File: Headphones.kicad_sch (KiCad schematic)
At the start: 34 parts, among them IC2 MAX9744ETH+T, IC3 UDA1334ATS_N2,118, U1 MOUDLE-SEEEDUINO-XIAO-ESP32C3

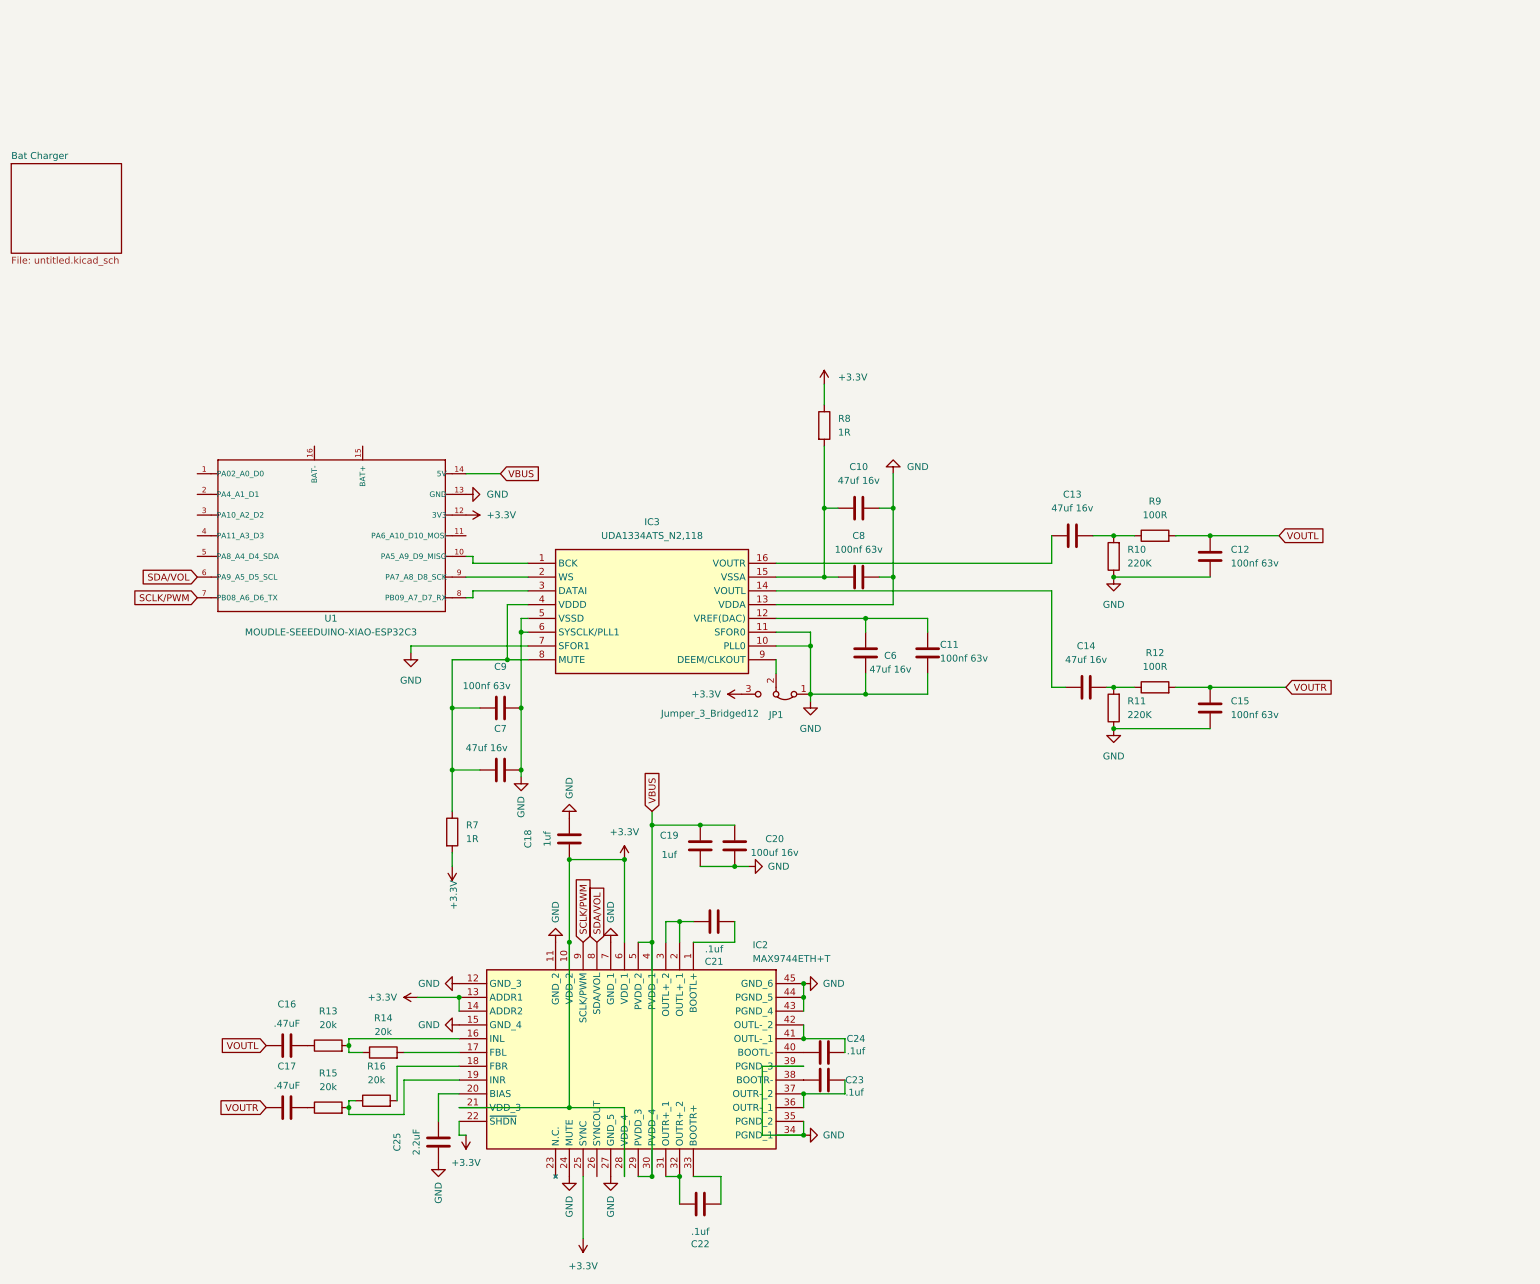
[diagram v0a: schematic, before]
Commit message: Minor updates
Might need more room for the esp32. With the new USB connector the board space is very tight
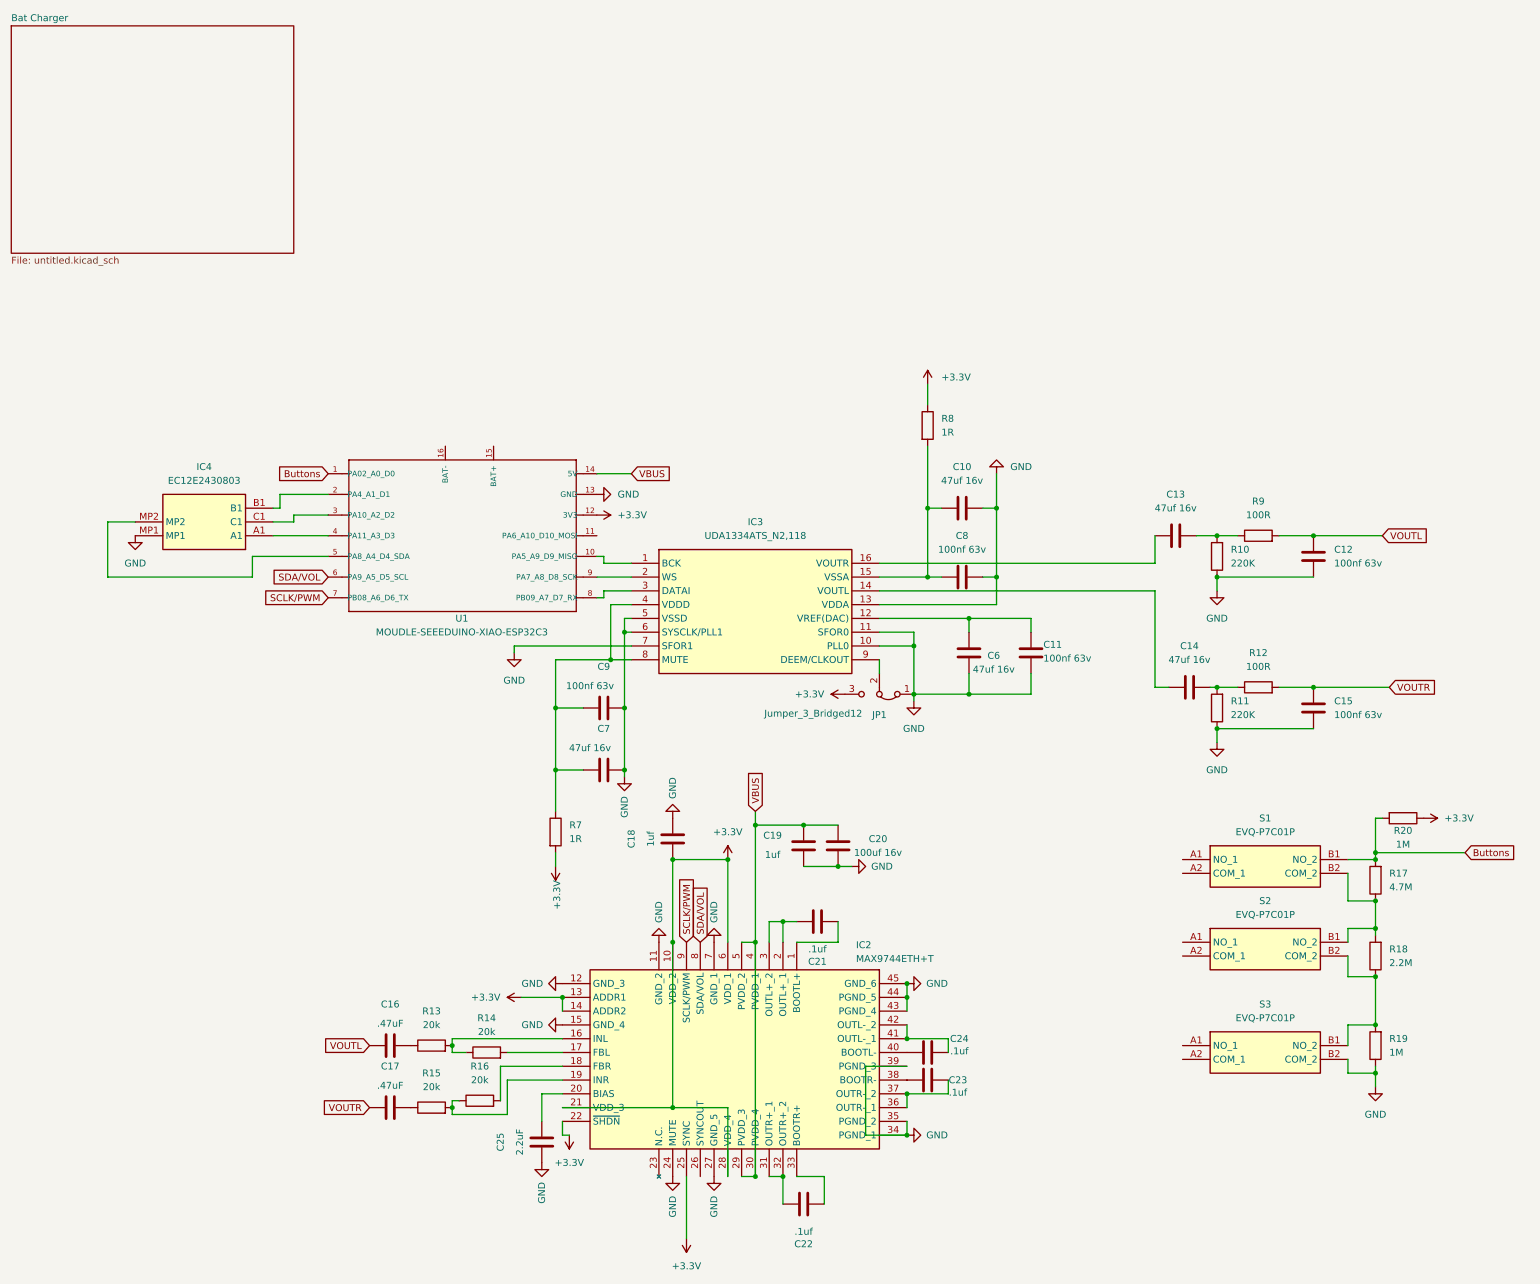
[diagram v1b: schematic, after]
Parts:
- added IC4: EC12E2430803, EC12E2430803, symbol SamacSys_Parts:EC12E2430803
- added R17: 4.7M, Resistor_SMD:R_0805_2012Metric, symbol Device:R
- added R18: 2.2M, Resistor_SMD:R_0805_2012Metric, symbol Device:R
- added R19, R20: 1M, Resistor_SMD:R_0805_2012Metric, symbol Device:R
- added S1, S2, S3: EVQ-P7C01P, EVQP7C01P, symbol SamacSys_Parts:EVQ-P7C01P
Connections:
- net +3.3V: now also R20.1
- net GND: now also IC4.MP1, R19.1, S3.B2 (COM_2)
- net Buttons: now reaches U1.1 (PA02_A0_D0)
- net Buttons: now also R17.2, R20.2, S1.B1 (NO_2)
- net at U1.2 (PA4_A1_D1): now also IC4.B1
- net at U1.3 (PA10_A2_D2): now also IC4.C1
- net at U1.4 (PA11_A3_D3): now also IC4.A1
- net at U1.5 (PA8_A4_D4_SDA): now also IC4.MP2
- new net: R18.1, R19.2, S2.B2 (COM_2), S3.B1 (NO_2)
- new net: R17.1, R18.2, S1.B2 (COM_2), S2.B1 (NO_2)
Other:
- moved on the sheet: C10, C11, C12, C13, C14, C15, C16, C17, C18, C19, C20, C21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

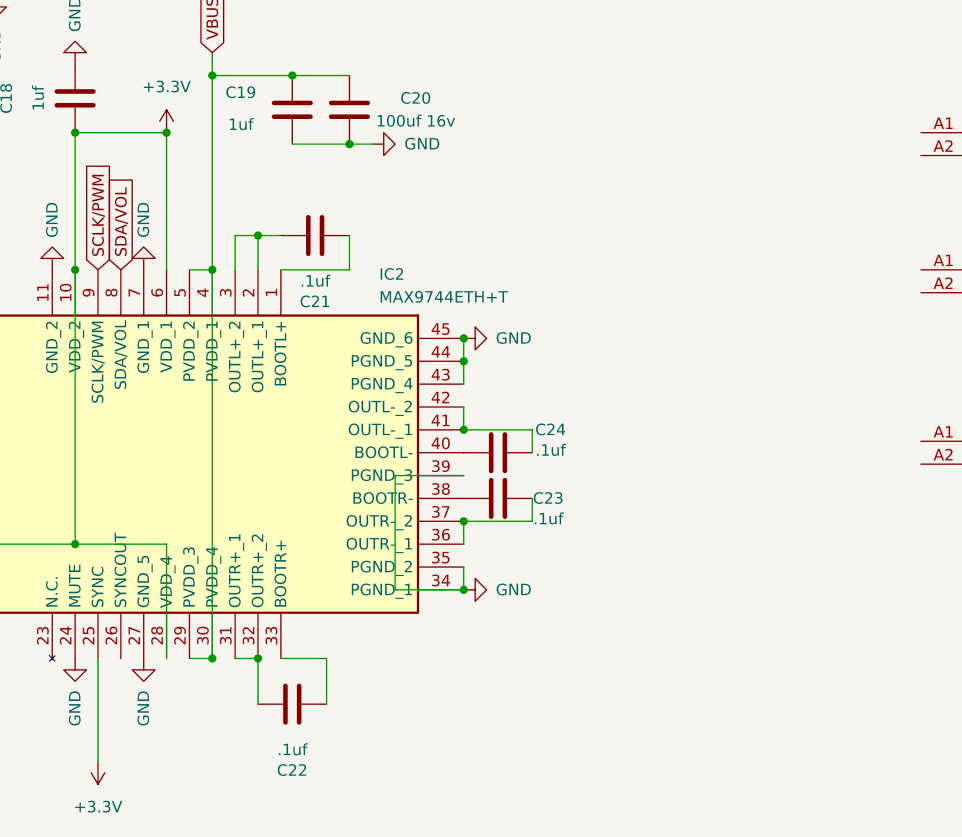
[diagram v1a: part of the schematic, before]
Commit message: Rev1 Update
Layout and traces done. 3d model done. Need to review layout placement and schematic. Change amp and dsp for lower cost??
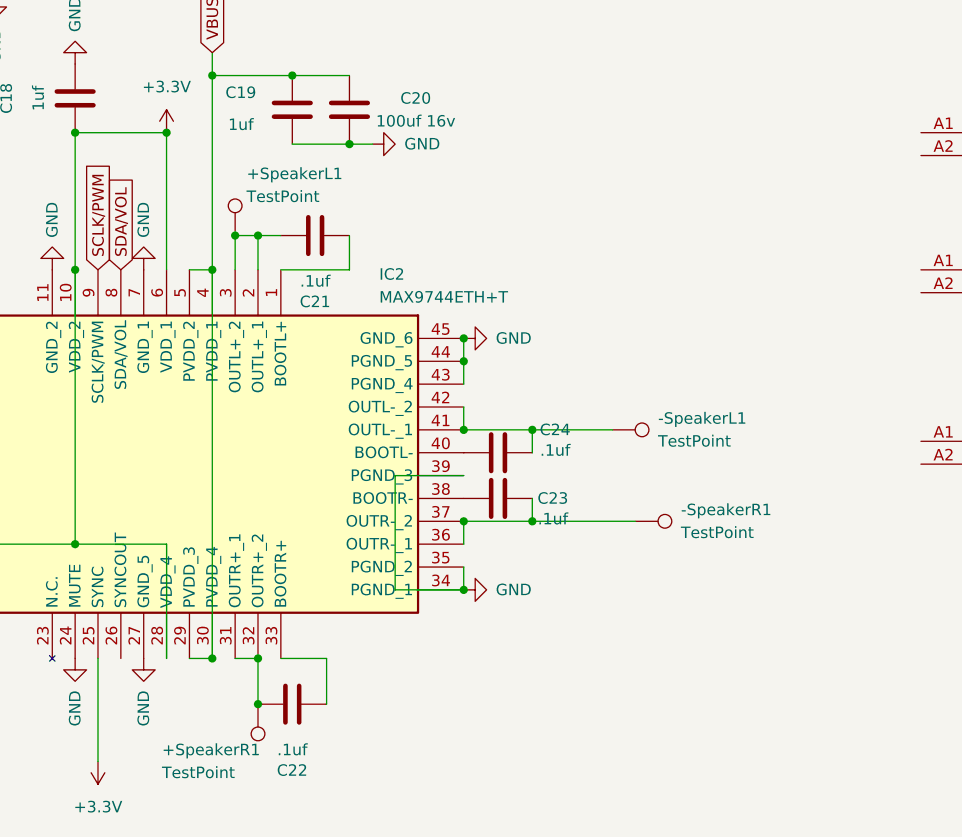
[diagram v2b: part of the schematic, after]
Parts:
- added +SpeakerL1, +SpeakerR1, -SpeakerL1, -SpeakerR1: TestPoint, TestPoint:TestPoint_Loop_D1.80mm_Drill1.0mm_Beaded, symbol Connector:TestPoint
- R7, R8: footprint Resistor_SMD:R_1206_3216Metric -> Resistor_SMD:R_0805_2012Metric
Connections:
- net at C21.2, IC2.2 (OUTL+_1), IC2.3 (OUTL+_2): now also +SpeakerL1.1
- net at C23.2, IC2.36 (OUTR-_1), IC2.37 (OUTR-_2): now also -SpeakerR1.1
- net at C22.2, IC2.31 (OUTR+_1), IC2.32 (OUTR+_2): now also +SpeakerR1.1
- net at C24.2, IC2.41 (OUTL-_1), IC2.42 (OUTL-_2): now also -SpeakerL1.1
